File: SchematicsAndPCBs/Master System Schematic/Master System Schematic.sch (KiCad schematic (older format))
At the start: 0 parts

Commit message: Master Schematic 1st revision
Added Full battery, TS, Shutdown, and BMS and Motor Controller
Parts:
- added BT1: 12V GLV Battery, symbol Device:Battery_Cell
- added D?: SSOK2, symbol Device:LED
- added D?: SSOK1, symbol Device:LED
- added D?: IMD_STATUS_OK LED, symbol Device:LED
- added D?: BMS_STATUS_OK LED, symbol Device:LED
- added D?: TRACTIVE SYSTEM ACTIVE LAMP, symbol Device:LED
- added F?: GLV Main Fuse, symbol Device:Fuse
- added F?: Shutdown Fuse, symbol Device:Fuse
- added F?: BMS Fuse, symbol Device:Fuse
- added F?: MC Fuse, symbol Device:Fuse
- added F? (x4): Fuse, symbol Device:Fuse
- added F?: IMD Fuse, symbol Device:Fuse
- added J1: GND, symbol Connector:Conn_01x01_Female
- added J2: TS+, symbol Connector:Conn_01x01_Female
- added J3: TS-, symbol Connector:Conn_01x01_Female
- added R?: 2.2k, symbol Device:R
- added RV?: ACCEL_POT, symbol Device:R_POT
- added RV?: BRAKE_POT, symbol Device:R_POT
- added SW? (x2): SideMounted (BRB), symbol Switch:SW_Push_Open
- added SW?: GLVMS, symbol Switch:SW_SPST
- added SW?: Brake Over-Travel Switch, symbol Switch:SW_SPST
- added SW?: Cockpit Shutdown (BRB), symbol Switch:SW_Push_Open
- added SW?: TSMS, symbol Switch:SW_SPST
- added SW?: RTDSwitch (latching), symbol Switch:SW_SPST
- added SW?: ChargeSwitch, symbol Switch:SW_SPST
- added SW?: BRAKE_SWITCH, symbol Switch:SW_SPST
- added U?: Bender_Isometer_IR155-3204, symbol NER_MASTERSYS_PART_LIBRARY:Bender_Isometer_IR155-3204
- added U?: Emrax228HV_Motor, symbol NER_MASTERSYS_PART_LIBRARY:Emrax228HV_Motor
- added U?: RinehartPM100DX_MotorController, symbol NER_MASTERSYS_PART_LIBRARY:RinehartPM100DX_MotorController
- added U?: OrionBMS2, symbol Full-Battery-System-rescue:OrionBMS2-FSAE_Components
- added U?: OrionCurrentSens, symbol Full-Battery-System-rescue:OrionCurrentSens-FSAE_Components
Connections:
- new net: BT1.1 (+), F?.1
- new net: F?.2, SW?.2 (B)
- new net: SW?.1 (A), SW?.2 (B) (x2)
- new net: F?.1, F?.1, F?.1, F?.1, F?.1, F?.1, F?.1, F?.1, SW?.1 (A)
- new net: D?.2 (A), D?.2 (A), F?.2, SW?.1 (A)
- new net: SW?.2 (B), SW?.2 (B)
- new net: F?.2, U?.23 (CANB_H), U?.8 (Reverse_Enable_Switch)
- new net: F?.2, U?.~ (STATUS_OK)
- new net: U?.~ (AC3), U?.~ (TS-) (x3)
- new net: RV?.3, U?.1 (Accel_Pedal_PWR)
- new net: RV?.2, U?.13 (Accel_Pedal_Wiper)
- new net: RV?.3, U?.14 (XDCR_PWR)
- new net: RV?.1, U?.15 (AGND)
- new net: RV?.1, U?.2 (Accel_Pedal_GND)
- new net: SW?.2 (B), U?.20 (Brake_Switch)
- new net: RV?.2, U?.25 (Brake_Pedal)
- new net: U?.L1 (Load+), U?.~ (TS-)
- new net: U?.2(B) (C_High), U?.C13 (C_High)
- new net: U?.4(D) (C_Low), U?.C14 (C_Low)
- new net: U?.3(C) (GND), U?.C27 (C_Sens_GND)
- new net: U?.1(A) (+5_Pow), U?.C28 (C_Sens)
- new net: SW?.1 (A), U?.IO2 (R_Power)
- new net: SW?.1 (A), U?.IO3 (C_Power)
- new net Accumulator Container/IMD_HV_SENSE+: U?.~ (STATUS_OK)
- new net Accumulator Container/IMD_HV_SENSE-: U?.~ (STATUS_OK)
- new net Accumulator Container/MotorController_Precharge_+: U?.21 (RLY1_PreCharge)
- new net Accumulator Container/TS+: U?.L2 (Load-)
- new net Accumulator Container/TS-: U?.~ (TS-)
- new net Accumulator Container/TSAL+: D?.2 (A)
- new net Accumulator Container/TSAL-: D?.1 (K)
- new net Accumulator Container/TSMP+: J2.1 (Pin_1)
- new net Accumulator Container/TSMP-: J3.1 (Pin_1)
- new net CHASSIS_GND: BT1.2 (-), D?.1 (K), D?.1 (K), J1.1 (Pin_1), R?.1, SW?.1 (A), U?.14 (XDCR_PWR), U?.6 (GND), U?.IO12 (GND), U?.~ (STATUS_OK)
- new net Charger/+12V: F?.2, SW?.2 (B), SW?.2 (B)
- new net Charger/CHARGER_SAFETY: U?.IO6 (C_Safety)
- new net LatchingStartStopController: SW?.1 (A)
- new net Shutdown Latching Circuits/BMSErrorIndicatorControl_IN: D?.1 (K)
- new net Shutdown Latching Circuits/BMS_Status: U?.IO26 (MPEnable)
- new net Shutdown Latching Circuits/IMDErrorIndicatorControl_IN: D?.1 (K)
- new net Shutdown Latching Circuits/IMD_Status: R?.2, U?.~ (STATUS_OK)
- new net Shutdown Latching Circuits/ShutdownLatch_Control_IN: SW?.2 (B)
- new net Shutdown Latching Circuits/ShutdownLatch_Control_OUT: D?.2 (A), D?.2 (A), SW?.1 (A)
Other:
- note added: "Fusebox for \nGLV Instruments"
- note added: "RTDS & LATCHING START"
- note added: "TSMPs"

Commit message: Updating Library References
Shifting references in the Master Schematic project to use the new NER library
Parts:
- removed D?: TRACTIVE SYSTEM ACTIVE LAMP, symbol Device:LED
- added U?: TSAL, symbol NER:TSAL
- U1: renamed from U?; symbol Full-Battery-System-rescue:OrionBMS2-FSAE_Components -> NER:OrionBMS2
- U?: symbol NER_MASTERSYS_PART_LIBRARY:Bender_Isometer_IR155-3204 -> NER:Bender_Isometer_IR155-3204
- U?: symbol NER_MASTERSYS_PART_LIBRARY:Emrax228HV_Motor -> NER:Emrax228HV_Motor
- U?: symbol NER_MASTERSYS_PART_LIBRARY:RinehartPM100DX_MotorController -> NER:RinehartPM100DX_MotorController
- U?: symbol Full-Battery-System-rescue:OrionCurrentSens-FSAE_Components -> NER:OrionCurrentSens
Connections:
- net Accumulator Container/TSAL+: now also U?.~ (DC_-)
- net Accumulator Container/TSAL-: now also U?.~ (DC_-)
- new net: F?.2, U?.23 (CANB_H), U?.8 (Reverse_Enable_Switch)
- new net: U?.~ (AC3), U?.~ (TS-) (x2)
- now unconnected: U?.23 (CANB_H), U?.8 (Reverse_Enable_Switch)
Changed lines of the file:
@@
 EESchema Schematic File Version 4
+LIBS:Master System Schematic-cache
 EELAYER 30 0
 EELAYER END
@@
 	4300 2200 4450 2200
 $Comp
-L NER_MASTERSYS_PART_LIBRARY:Emrax228HV_Motor U?
+L NER:Emrax228HV_Motor U?
 U 1 1 5F972C2B
 P 10650 5800
@@
 $EndComp
 $Comp
-L NER_MASTERSYS_PART_LIBRARY:RinehartPM100DX_MotorController U?
+L NER:RinehartPM100DX_MotorController U?
 U 1 1 5F97D518
 P 10100 5500
@@
 $EndComp
 $Comp
-L NER_MASTERSYS_PART_LIBRARY:Bender_Isometer_IR155-3204 U?
+L NER:Bender_Isometer_IR155-3204 U?
 U 1 1 5F94A015
 P 4100 3650
@@
 Wire Wire Line
 	3250 4350 3250 4000
-$Comp
-L Device:LED D?
-U 1 1 605F9012
-P 2400 6100
-F 0 "D?" H 2400 5850 50  0000 C CNN
-F 1 "TRACTIVE SYSTEM ACTIVE LAMP" H 2400 5950 50  0000 C CNN
-F 2 "" H 2400 6100 50  0001 C CNN
-F 3 "~" H 2400 6100 50  0001 C CNN
-	1    2400 6100
-	1    0    0    1
-$EndComp
-Wire Wire Line
-	2550 6100 3200 6100
-Wire Wire Line
-	2250 6100 2200 6100
-Wire Wire Line
-	2200 6100 2200 6200
 Wire Bus Line
 	4950 6800 5050 6800
@@
 Connection ~ 5050 6150
 $Comp
-L Full-Battery-System-rescue:OrionBMS2-FSAE_Components U?
+L NER:OrionBMS2 U1
 U 1 1 606C5173
 P 7450 3400
-F 0 "U?" H 7450 700 50  0000 C CNN
+F 0 "U1" H 7450 700 50  0000 C CNN
 F 1 "OrionBMS2" H 7450 600 50  0000 C CNN
 F 2 "" H 7450 3400 50  0001 C CNN
@@
 	6300 4100 6300 5000
 $Comp
-L Full-Battery-System-rescue:OrionCurrentSens-FSAE_Components U?
+L NER:OrionCurrentSens U?
 U 1 1 6111F589
 P 5900 7700
@@
 Wire Wire Line
 	1450 850  1450 2900
-Wire Wire Line
-	2200 6200 3200 6200
 Wire Notes Line
 	8800 1950 10950 1950
@@
 Text Notes 8800 1000 0    50   ~ 0
 RTDS & LATCHING START
+$Comp
+L NER:TSAL U?
+U 1 1 5F652630
+P 2450 5950
+F 0 "U?" H 2342 6075 50  0000 C CNN
+F 1 "TSAL" H 2342 5984 50  0000 C CNN
+F 2 "" H 2450 5950 50  0001 C CNN
+F 3 "" H 2450 5950 50  0001 C CNN
+	1    2450 5950
+	-1   0    0    -1
+$EndComp
+Wire Wire Line
+	3200 6100 2900 6100
+Wire Wire Line
+	2900 6100 2900 6050
+Wire Wire Line
+	2900 6050 2750 6050
+Wire Wire Line
+	2750 6250 2900 6250
+Wire Wire Line
+	2900 6250 2900 6200
+Wire Wire Line
+	2900 6200 3200 6200
 $EndSCHEMATC

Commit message: Paper Size and Title Blocks
-Switched all paper sizes over to America units  (letter size A and tabloid size B) (so we can actually be cool and print them an stuff)
-Fixed title blocks to use sheet properties
-Started some changes to the accumulator segment schematic
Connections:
- new net: F?.2, U?.23 (CANB_H), U?.8 (Reverse_Enable_Switch)
- new net: U?.~ (AC3), U?.~ (TS-) (x2)
- now unconnected: U?.23 (CANB_H), U?.8 (Reverse_Enable_Switch)
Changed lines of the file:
@@
 EELAYER 30 0
 EELAYER END
-$Descr A4 11693 8268
+$Descr B 17000 11000
 encoding utf-8
 Sheet 1 8
 Title "NER FH 2020-2021 Master Electrical Schematic"
-Date "2020-08-25"
-Rev "1"
+Date "2020-09-17"
+Rev "2"
 Comp "Northeastern Electric Racing"
 Comment1 "Dylan Gardner, Matthew McCauley"

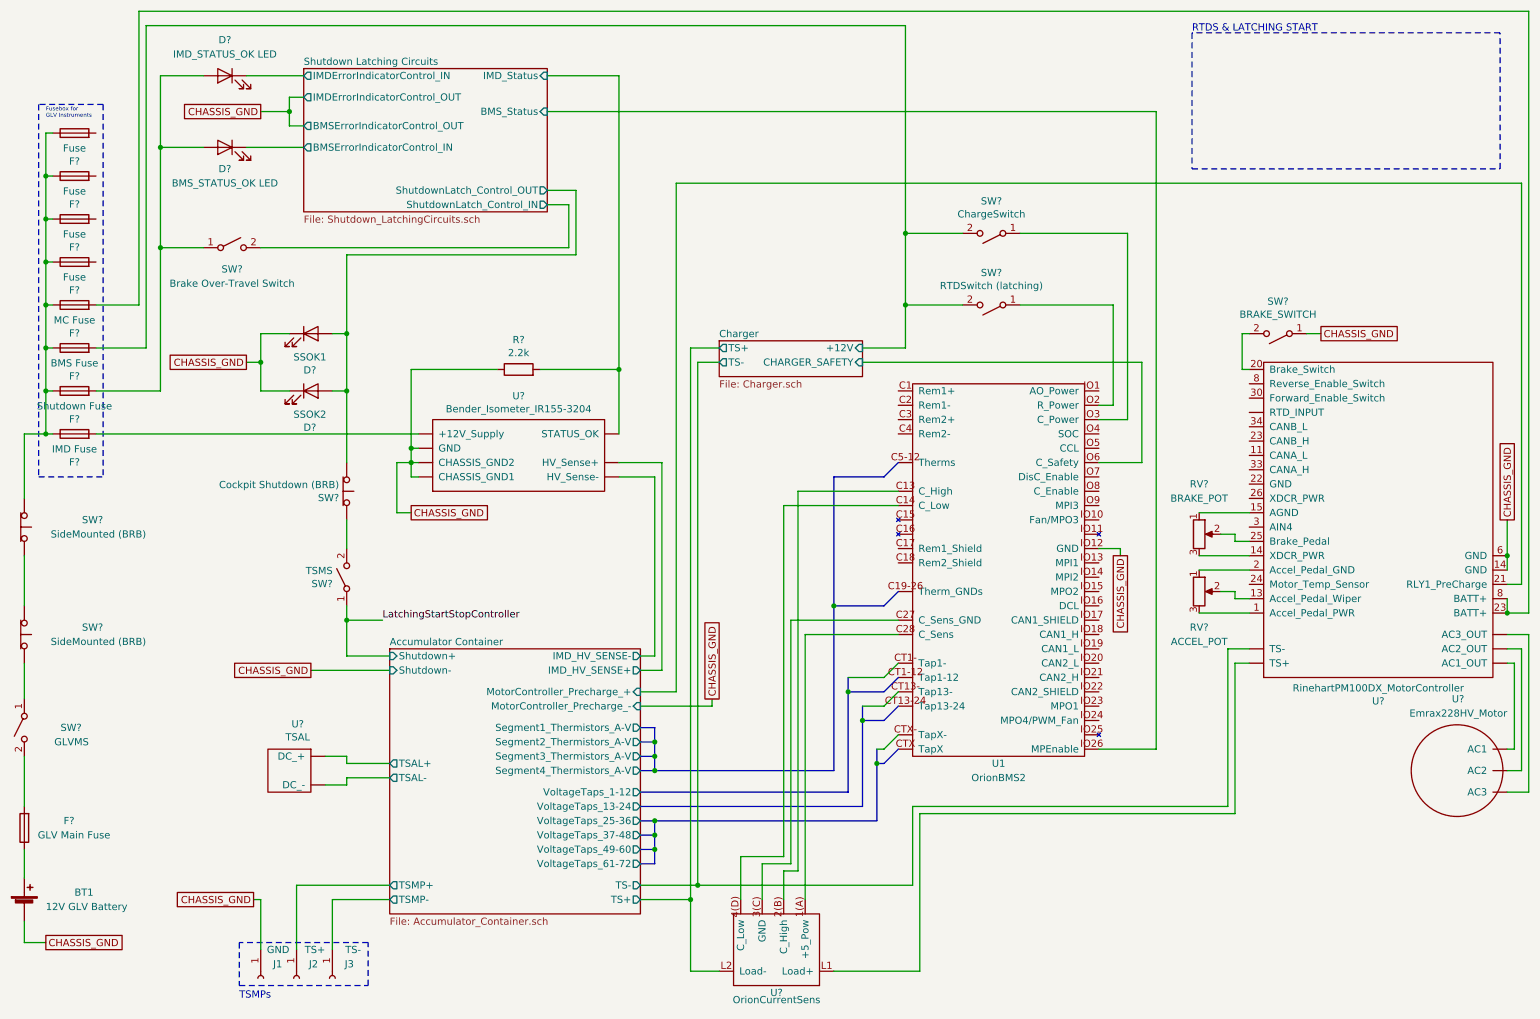
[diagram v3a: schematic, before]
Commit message: Therms and Volt Taps
Mostly fixed all thermistor and volt taps
Also created new sheet for BMS container and updated library part for OrionThermExpansionModule
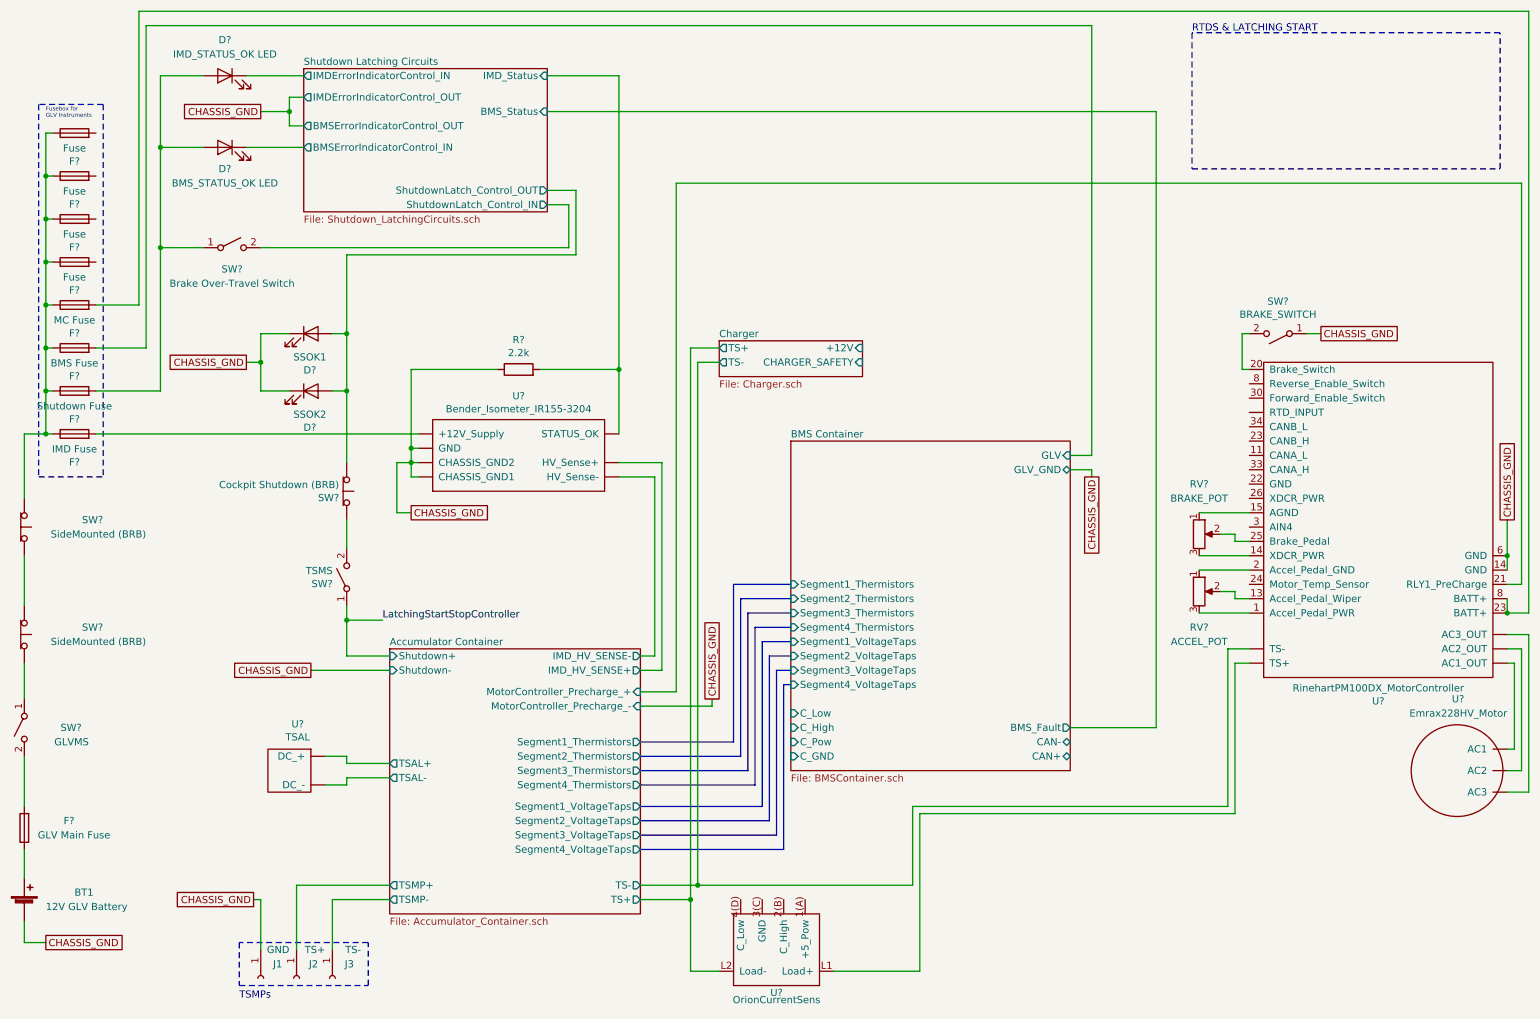
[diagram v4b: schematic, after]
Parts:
- removed SW?: RTDSwitch (latching), symbol Switch:SW_SPST
- removed SW?: ChargeSwitch, symbol Switch:SW_SPST
- removed U1: OrionBMS2, symbol NER:OrionBMS2
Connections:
- net Charger/+12V: no longer F?.2
- new net: F?.2, U?.23 (CANB_H), U?.8 (Reverse_Enable_Switch)
- new net: U?.~ (AC3), U?.~ (TS-) (x2)
- new net BMS Container/GLV: F?.2
- now unconnected: U?.23 (CANB_H), U?.8 (Reverse_Enable_Switch)
